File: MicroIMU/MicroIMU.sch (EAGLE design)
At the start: 18 parts, among them IC1 LSM303DLHC

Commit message: Done routing
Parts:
- renumbered 15V to +15V
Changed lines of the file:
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@@
 <part name="C3" library="resistor" deviceset="C-EU" device="C0402" value="0.01 uF"/>
 <part name="GND" library="wirepad" deviceset="1,6/0,8" device="" value="GND"/>
-<part name="15V" library="wirepad" deviceset="1,6/0,8" device="" value="15V"/>
+<part name="+15V" library="wirepad" deviceset="1,6/0,8" device="" value="15V"/>
 <part name="SDA" library="wirepad" deviceset="1,6/0,8" device="" value="SDA"/>
 <part name="P+1" library="supply1" deviceset="+15V" device=""/>
@@
 <instance part="C3" gate="G$1" x="144.78" y="185.42"/>
 <instance part="GND" gate="P" x="86.36" y="119.38"/>
-<instance part="15V" gate="P" x="86.36" y="127"/>
+<instance part="+15V" gate="P" x="86.36" y="127"/>
 <instance part="SDA" gate="P" x="86.36" y="144.78"/>
 <instance part="P+1" gate="1" x="99.06" y="134.62"/>
@@
 </segment>
 <segment>
-<pinref part="15V" gate="P" pin="P"/>
+<pinref part="+15V" gate="P" pin="P"/>
 <wire x1="88.9" y1="127" x2="99.06" y2="127" width="0.1524" layer="91"/>
 <pinref part="P+1" gate="1" pin="+15V"/>

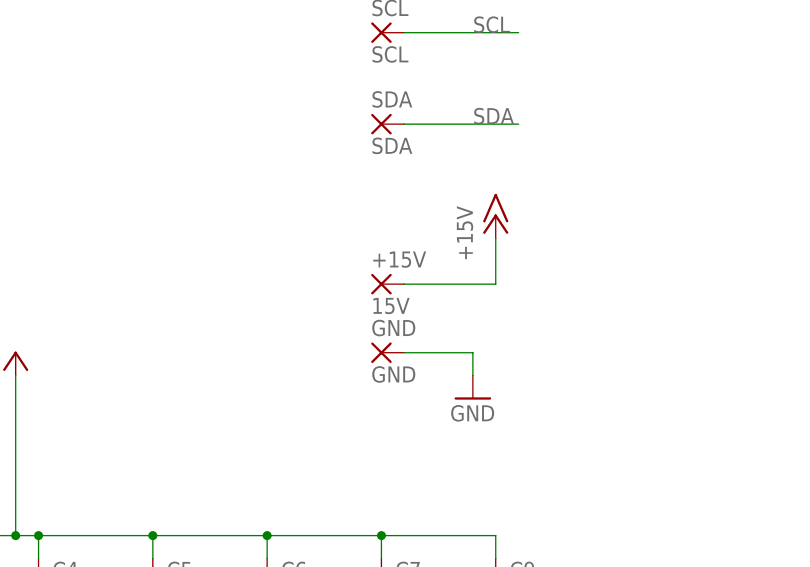
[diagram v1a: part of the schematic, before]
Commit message: Galen made minor layout changes to save space
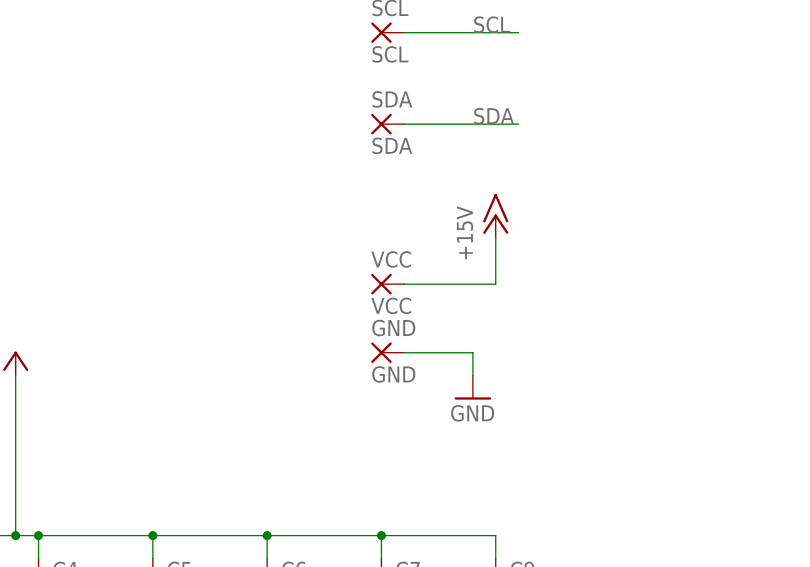
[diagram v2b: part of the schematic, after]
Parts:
- VCC: value 15V -> VCC
- renumbered +15V to VCC
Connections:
- net +15V renamed VCC
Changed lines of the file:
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@@
 <part name="C3" library="resistor" deviceset="C-EU" device="C0402" value="0.01 uF"/>
 <part name="GND" library="wirepad" deviceset="1,6/0,8" device="" value="GND"/>
-<part name="+15V" library="wirepad" deviceset="1,6/0,8" device="" value="15V"/>
+<part name="VCC" library="wirepad" deviceset="1,6/0,8" device="" value="VCC"/>
 <part name="SDA" library="wirepad" deviceset="1,6/0,8" device="" value="SDA"/>
 <part name="P+1" library="supply1" deviceset="+15V" device=""/>
@@
 <instance part="C3" gate="G$1" x="144.78" y="185.42"/>
 <instance part="GND" gate="P" x="86.36" y="119.38"/>
-<instance part="+15V" gate="P" x="86.36" y="127"/>
+<instance part="VCC" gate="P" x="86.36" y="127"/>
 <instance part="SDA" gate="P" x="86.36" y="144.78"/>
 <instance part="P+1" gate="1" x="99.06" y="134.62"/>
@@
 </busses>
 <nets>
-<net name="+15V" class="0">
+<net name="VCC" class="0">
 <segment>
 <pinref part="U$2" gate="G$1" pin="IN"/>
@@
 </segment>
 <segment>
-<pinref part="+15V" gate="P" pin="P"/>
+<pinref part="VCC" gate="P" pin="P"/>
 <wire x1="88.9" y1="127" x2="99.06" y2="127" width="0.1524" layer="91"/>
 <pinref part="P+1" gate="1" pin="+15V"/>

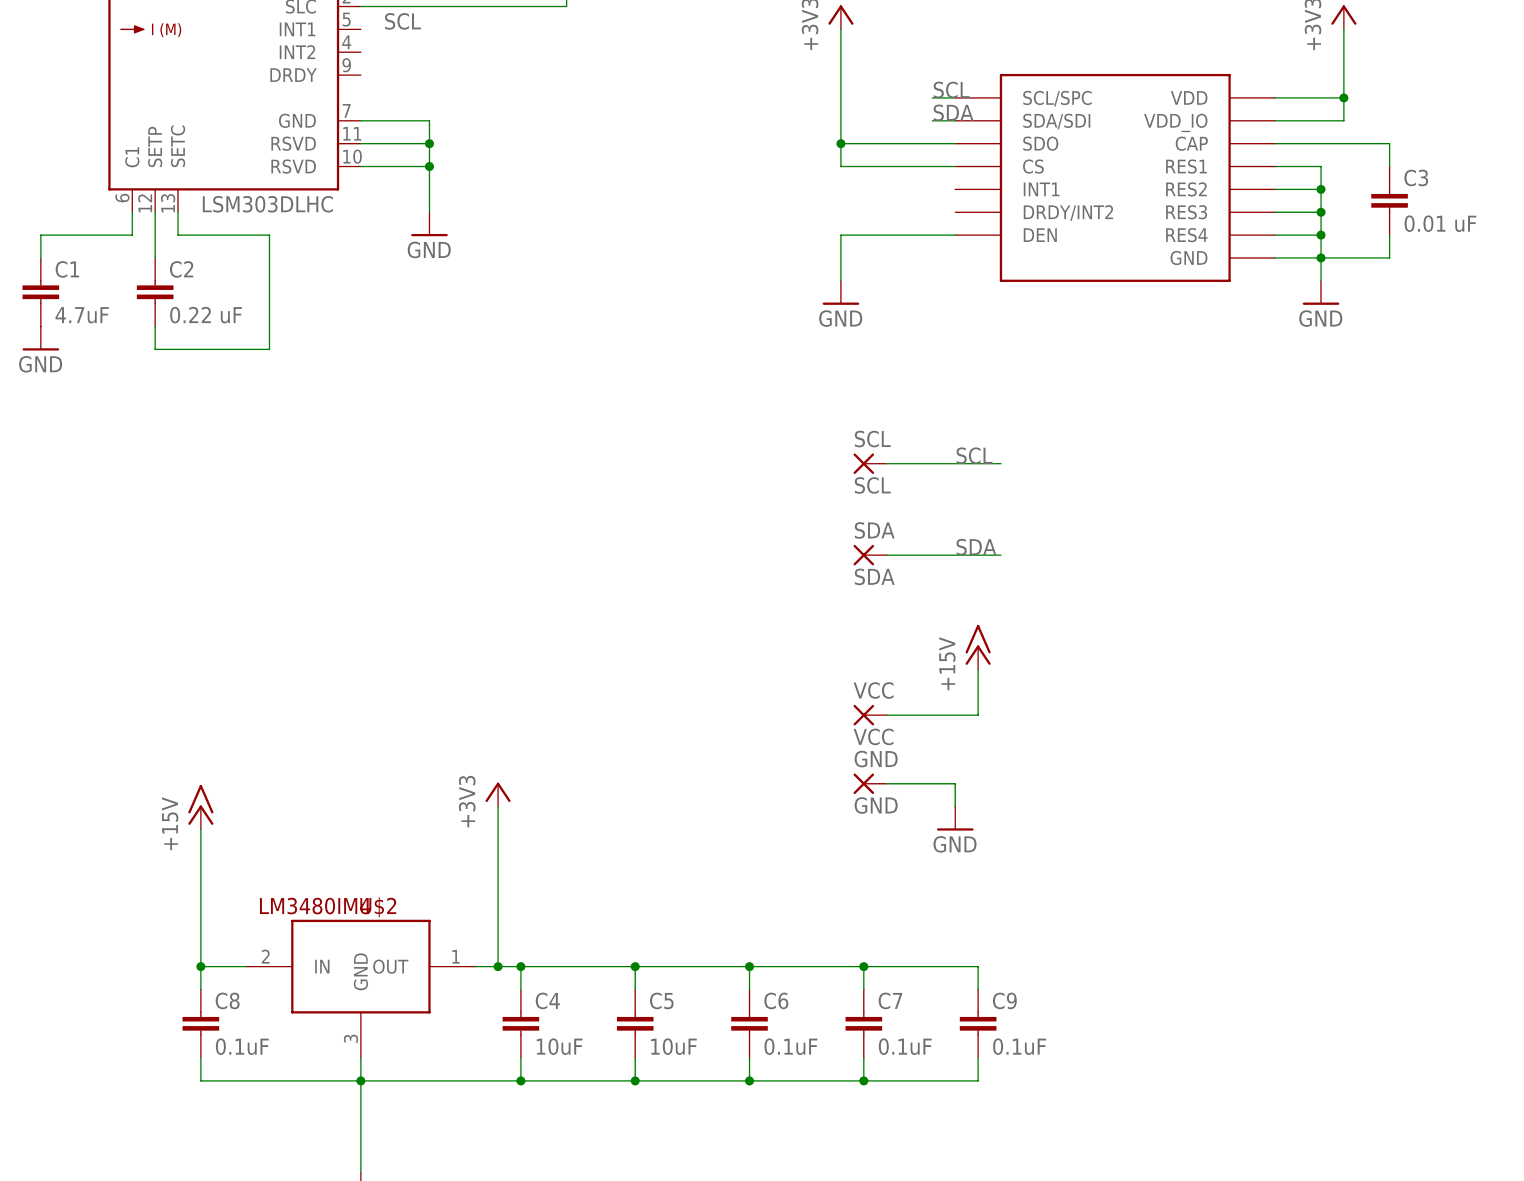
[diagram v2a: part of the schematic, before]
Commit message: Added labels to silkscreen layer
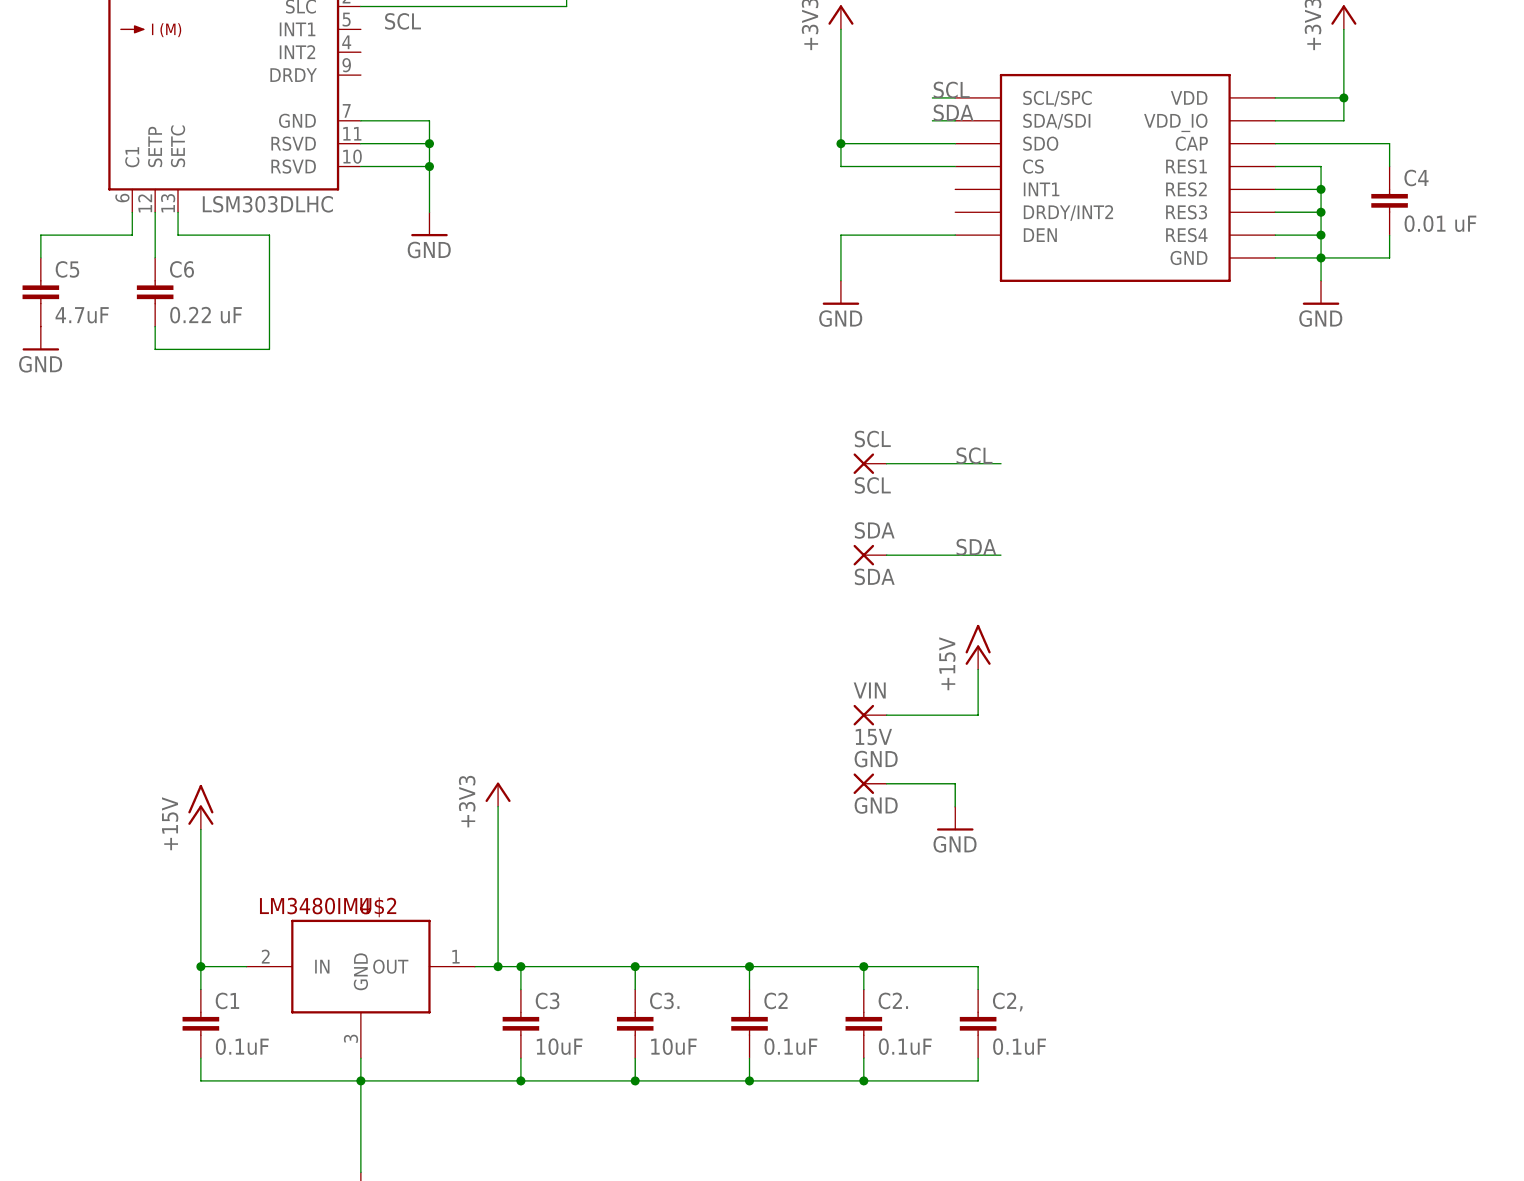
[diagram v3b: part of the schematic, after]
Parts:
- removed C8: 0.1uF, resistor:C-EUC0201
- added C3.: 10uF, resistor:C-EUC0603
- C1: value 4.7uF -> 0.1uF; device resistor:C-EUC0402 -> resistor:C-EUC0201
- C2: value 0.22 uF -> 0.1uF
- C3: value 0.01 uF -> 10uF; device resistor:C-EUC0402 -> resistor:C-EUC0603
- C4: value 10uF -> 0.01 uF; device resistor:C-EUC0603 -> resistor:C-EUC0402
- C5: value 10uF -> 4.7uF; device resistor:C-EUC0603 -> resistor:C-EUC0402
- C6: value 0.1uF -> 0.22 uF
- VIN: value VCC -> 15V
- renumbered C7 to C2., C9 to C2,, VCC to VIN
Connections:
- removed net VCC: C8.1, U$2.IN, VIN.P
- new net +15V: C1.1, U$2.IN, VIN.P
- net +3V3: now also C2.1, C3..1, C3.1; no longer C4.1, C5.1, C6.1
- net GND: now also C2.2, C3..2; no longer C6.2, C8.2
- net N$1: now also C5.1; no longer C1.1
- net N$2: now also C6.1; no longer C2.1
- net N$3: now also C6.2; no longer C2.2
- net N$9: now also C4.1; no longer C3.1
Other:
- moved on the sheet: C1, C2, C3, C4, C5, C6
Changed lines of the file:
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@@
 <part name="R2" library="resistor" deviceset="R-US_" device="R0201" value="10k"/>
 <part name="+3V3" library="supply1" deviceset="+3V3" device=""/>
-<part name="C1" library="resistor" deviceset="C-EU" device="C0402" value="4.7uF"/>
+<part name="C5" library="resistor" deviceset="C-EU" device="C0402" value="4.7uF"/>
 <part name="GND4" library="supply1" deviceset="GND" device=""/>
-<part name="C2" library="resistor" deviceset="C-EU" device="C0201" value="0.22 uF"/>
+<part name="C6" library="resistor" deviceset="C-EU" device="C0201" value="0.22 uF"/>
 <part name="+3V4" library="supply1" deviceset="+3V3" device=""/>
 <part name="GND6" library="supply1" deviceset="GND" device=""/>
-<part name="C3" library="resistor" deviceset="C-EU" device="C0402" value="0.01 uF"/>
+<part name="C4" library="resistor" deviceset="C-EU" device="C0402" value="0.01 uF"/>
 <part name="GND" library="wirepad" deviceset="1,6/0,8" device="" value="GND"/>
-<part name="VCC" library="wirepad" deviceset="1,6/0,8" device="" value="VCC"/>
+<part name="VIN" library="wirepad" deviceset="1,6/0,8" device="" value="15V"/>
 <part name="SDA" library="wirepad" deviceset="1,6/0,8" device="" value="SDA"/>
 <part name="P+1" library="supply1" deviceset="+15V" device=""/>
 <part name="SCL" library="wirepad" deviceset="1,6/0,8" device="" value="SCL"/>
 <part name="GND5" library="supply1" deviceset="GND" device=""/>
-<part name="C4" library="resistor" deviceset="C-EU" device="C0603" value="10uF"/>
-<part name="C5" library="resistor" deviceset="C-EU" device="C0603" value="10uF"/>
-<part name="C6" library="resistor" deviceset="C-EU" device="C0201" value="0.1uF"/>
-<part name="C7" library="resistor" deviceset="C-EU" device="C0201" value="0.1uF"/>
-<part name="C8" library="resistor" deviceset="C-EU" device="C0201" value="0.1uF"/>
-<part name="C9" library="resistor" deviceset="C-EU" device="C0201" value="0.1uF"/>
+<part name="C3" library="resistor" deviceset="C-EU" device="C0603" value="10uF"/>
+<part name="C3." library="resistor" deviceset="C-EU" device="C0603" value="10uF"/>
+<part name="C2" library="resistor" deviceset="C-EU" device="C0201" value="0.1uF"/>
+<part name="C2." library="resistor" deviceset="C-EU" device="C0201" value="0.1uF"/>
+<part name="C1" library="resistor" deviceset="C-EU" device="C0201" value="0.1uF"/>
+<part name="C2," library="resistor" deviceset="C-EU" device="C0201" value="0.1uF"/>
 </parts>
 <sheets>
@@
 <instance part="R2" gate="G$1" x="53.34" y="213.36" rot="R90"/>
 <instance part="+3V3" gate="G$1" x="35.56" y="231.14"/>
-<instance part="C1" gate="G$1" x="-5.08" y="175.26"/>
+<instance part="C5" gate="G$1" x="-5.08" y="175.26"/>
 <instance part="GND4" gate="1" x="-5.08" y="167.64"/>
-<instance part="C2" gate="G$1" x="7.62" y="175.26"/>
+<instance part="C6" gate="G$1" x="7.62" y="175.26"/>
 <instance part="+3V4" gate="G$1" x="83.82" y="205.74"/>
 <instance part="GND6" gate="1" x="83.82" y="172.72"/>
-<instance part="C3" gate="G$1" x="144.78" y="185.42"/>
+<instance part="C4" gate="G$1" x="144.78" y="185.42"/>
 <instance part="GND" gate="P" x="86.36" y="119.38"/>
-<instance part="VCC" gate="P" x="86.36" y="127"/>
+<instance part="VIN" gate="P" x="86.36" y="127"/>
 <instance part="SDA" gate="P" x="86.36" y="144.78"/>
 <instance part="P+1" gate="1" x="99.06" y="134.62"/>
 <instance part="SCL" gate="P" x="86.36" y="154.94"/>
 <instance part="GND5" gate="1" x="96.52" y="114.3"/>
-<instance part="C4" gate="G$1" x="48.26" y="93.98"/>
-<instance part="C5" gate="G$1" x="60.96" y="93.98"/>
-<instance part="C6" gate="G$1" x="73.66" y="93.98"/>
-<instance part="C7" gate="G$1" x="86.36" y="93.98"/>
-<instance part="C8" gate="G$1" x="12.7" y="93.98"/>
-<instance part="C9" gate="G$1" x="99.06" y="93.98"/>
+<instance part="C3" gate="G$1" x="48.26" y="93.98"/>
+<instance part="C3." gate="G$1" x="60.96" y="93.98"/>
+<instance part="C2" gate="G$1" x="73.66" y="93.98"/>
+<instance part="C2." gate="G$1" x="86.36" y="93.98"/>
+<instance part="C1" gate="G$1" x="12.7" y="93.98"/>
+<instance part="C2," gate="G$1" x="99.06" y="93.98"/>
 </instances>
 <busses>
 </busses>
 <nets>
-<net name="VCC" class="0">
+<net name="+15V" class="0">
 <segment>
 <pinref part="U$2" gate="G$1" pin="IN"/>
@@
 <pinref part="P+2" gate="1" pin="+15V"/>
 <wire x1="12.7" y1="99.06" x2="12.7" y2="114.3" width="0.1524" layer="91"/>
-<pinref part="C8" gate="G$1" pin="1"/>
+<pinref part="C1" gate="G$1" pin="1"/>
 <wire x1="12.7" y1="96.52" x2="12.7" y2="99.06" width="0.1524" layer="91"/>
 <junction x="12.7" y="99.06"/>
 </segment>
 <segment>
-<pinref part="VCC" gate="P" pin="P"/>
+<pinref part="VIN" gate="P" pin="P"/>
 <wire x1="88.9" y1="127" x2="99.06" y2="127" width="0.1524" layer="91"/>
 <pinref part="P+1" gate="1" pin="+15V"/>
@@
 <pinref part="GND2" gate="1" pin="GND"/>
 <wire x1="30.48" y1="88.9" x2="30.48" y2="86.36" width="0.1524" layer="91"/>
-<pinref part="C4" gate="G$1" pin="2"/>
+<pinref part="C3" gate="G$1" pin="2"/>
 <wire x1="30.48" y1="86.36" x2="30.48" y2="76.2" width="0.1524" layer="91"/>
 <wire x1="48.26" y1="88.9" x2="48.26" y2="86.36" width="0.1524" layer="91"/>
 <wire x1="48.26" y1="86.36" x2="30.48" y2="86.36" width="0.1524" layer="91"/>
 <junction x="30.48" y="86.36"/>
-<pinref part="C5" gate="G$1" pin="2"/>
+<pinref part="C3." gate="G$1" pin="2"/>
 <wire x1="60.96" y1="88.9" x2="60.96" y2="86.36" width="0.1524" layer="91"/>
 <wire x1="60.96" y1="86.36" x2="48.26" y2="86.36" width="0.1524" layer="91"/>
 <junction x="48.26" y="86.36"/>
-<pinref part="C6" gate="G$1" pin="2"/>
+<pinref part="C2" gate="G$1" pin="2"/>
 <wire x1="73.66" y1="88.9" x2="73.66" y2="86.36" width="0.1524" layer="91"/>
 <wire x1="73.66" y1="86.36" x2="60.96" y2="86.36" width="0.1524" layer="91"/>
 <junction x="60.96" y="86.36"/>
-<pinref part="C7" gate="G$1" pin="2"/>
+<pinref part="C2." gate="G$1" pin="2"/>
 <wire x1="86.36" y1="88.9" x2="86.36" y2="86.36" width="0.1524" layer="91"/>
 <wire x1="86.36" y1="86.36" x2="73.66" y2="86.36" width="0.1524" layer="91"/>
 <junction x="73.66" y="86.36"/>
-<pinref part="C8" gate="G$1" pin="2"/>
+<pinref part="C1" gate="G$1" pin="2"/>
 <wire x1="12.7" y1="88.9" x2="12.7" y2="86.36" width="0.1524" layer="91"/>
 <wire x1="12.7" y1="86.36" x2="30.48" y2="86.36" width="0.1524" layer="91"/>
-<pinref part="C9" gate="G$1" pin="2"/>
+<pinref part="C2," gate="G$1" pin="2"/>
 <wire x1="99.06" y1="88.9" x2="99.06" y2="86.36" width="0.1524" layer="91"/>
 <wire x1="99.06" y1="86.36" x2="86.36" y2="86.36" width="0.1524" layer="91"/>
@@
 <wire x1="137.16" y1="187.96" x2="137.16" y2="185.42" width="0.1524" layer="91"/>
 <junction x="137.16" y="185.42"/>
-<pinref part="C3" gate="G$1" pin="2"/>
+<pinref part="C4" gate="G$1" pin="2"/>
 <wire x1="144.78" y1="180.34" x2="144.78" y2="177.8" width="0.1524" layer="91"/>
 <wire x1="144.78" y1="177.8" x2="137.16" y2="177.8" width="0.1524" layer="91"/>
@@
 </segment>
 <segment>
-<pinref part="C1" gate="G$1" pin="2"/>
+<pinref part="C5" gate="G$1" pin="2"/>
 <pinref part="GND4" gate="1" pin="GND"/>
 </segment>
@@
 <pinref part="U$2" gate="G$1" pin="OUT"/>
 <wire x1="43.18" y1="99.06" x2="45.72" y2="99.06" width="0.1524" layer="91"/>
-<pinref part="C4" gate="G$1" pin="1"/>
+<pinref part="C3" gate="G$1" pin="1"/>
 <wire x1="48.26" y1="96.52" x2="48.26" y2="99.06" width="0.1524" layer="91"/>
 <wire x1="48.26" y1="99.06" x2="45.72" y2="99.06" width="0.1524" layer="91"/>
 <junction x="45.72" y="99.06"/>
-<pinref part="C5" gate="G$1" pin="1"/>
+<pinref part="C3." gate="G$1" pin="1"/>
 <wire x1="60.96" y1="96.52" x2="60.96" y2="99.06" width="0.1524" layer="91"/>
 <wire x1="60.96" y1="99.06" x2="48.26" y2="99.06" width="0.1524" layer="91"/>
 <junction x="48.26" y="99.06"/>
-<pinref part="C6" gate="G$1" pin="1"/>
+<pinref part="C2" gate="G$1" pin="1"/>
 <wire x1="73.66" y1="96.52" x2="73.66" y2="99.06" width="0.1524" layer="91"/>
 <wire x1="73.66" y1="99.06" x2="60.96" y2="99.06" width="0.1524" layer="91"/>
 <junction x="60.96" y="99.06"/>
-<pinref part="C7" gate="G$1" pin="1"/>
+<pinref part="C2." gate="G$1" pin="1"/>
 <wire x1="86.36" y1="96.52" x2="86.36" y2="99.06" width="0.1524" layer="91"/>
 <wire x1="86.36" y1="99.06" x2="73.66" y2="99.06" width="0.1524" layer="91"/>
@@
 <wire x1="86.36" y1="99.06" x2="99.06" y2="99.06" width="0.1524" layer="91"/>
 <junction x="86.36" y="99.06"/>
-<pinref part="C9" gate="G$1" pin="1"/>
+<pinref part="C2," gate="G$1" pin="1"/>
 <wire x1="99.06" y1="99.06" x2="99.06" y2="96.52" width="0.1524" layer="91"/>
 </segment>
@@
 <segment>
 <pinref part="IC1" gate="G$1" pin="SETP"/>
-<pinref part="C2" gate="G$1" pin="1"/>
+<pinref part="C6" gate="G$1" pin="1"/>
 <wire x1="7.62" y1="182.88" x2="7.62" y2="177.8" width="0.1524" layer="91"/>
 </segment>
@@
 <wire x1="20.32" y1="180.34" x2="20.32" y2="167.64" width="0.1524" layer="91"/>
 <wire x1="20.32" y1="167.64" x2="7.62" y2="167.64" width="0.1524" layer="91"/>
-<pinref part="C2" gate="G$1" pin="2"/>
+<pinref part="C6" gate="G$1" pin="2"/>
 <wire x1="7.62" y1="167.64" x2="7.62" y2="170.18" width="0.1524" layer="91"/>
 </segment>
@@
 <wire x1="5.08" y1="182.88" x2="5.08" y2="180.34" width="0.1524" layer="91"/>
 <wire x1="5.08" y1="180.34" x2="-5.08" y2="180.34" width="0.1524" layer="91"/>
-<pinref part="C1" gate="G$1" pin="1"/>
+<pinref part="C5" gate="G$1" pin="1"/>
 <wire x1="-5.08" y1="180.34" x2="-5.08" y2="177.8" width="0.1524" layer="91"/>
 </segment>
@@
 <pinref part="U$1" gate="G$1" pin="CAP"/>
 <wire x1="132.08" y1="190.5" x2="144.78" y2="190.5" width="0.1524" layer="91"/>
-<pinref part="C3" gate="G$1" pin="1"/>
+<pinref part="C4" gate="G$1" pin="1"/>
 <wire x1="144.78" y1="190.5" x2="144.78" y2="187.96" width="0.1524" layer="91"/>
 </segment>
